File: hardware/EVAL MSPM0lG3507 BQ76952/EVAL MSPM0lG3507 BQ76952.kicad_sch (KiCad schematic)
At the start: 68 parts, among them J1 Conn_01x09_Socket, J10 Screw_Terminal_01x02, J11 Screw_Terminal_01x02, J12 Screw_Terminal_01x02, J13 Screw_Terminal_01x02, J14 Screw_Terminal_01x02, J17 Conn_02x02_Odd_Even, J2 Conn_02x05_Odd_Even, J3 Conn_01x04_Pin, J4 Screw_Terminal_01x02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

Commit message: partial correctinos to kicad
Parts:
- removed D6: LED, LED_SMD:LED_0805_2012Metric_Pad1.15x1.40mm_HandSolder, symbol Device:LED
- added D4: LED, LED_SMD:LED_0603_1608Metric, symbol Device:LED
- D1: footprint LED_SMD:LED_0201_0603Metric_Pad0.64x0.40mm_HandSolder -> LED_SMD:LED_0603_1608Metric; unit x10 0.12 -> 0.118
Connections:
- net -BATT: now also D4.1 (K)
- net at R3.2: now also D4.2 (A)
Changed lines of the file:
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@@
 			)
 		)
-		(property "Footprint" "LED_SMD:LED_0201_0603Metric_Pad0.64x0.40mm_HandSolder"
+		(property "Footprint" "LED_SMD:LED_0603_1608Metric"
 			(at 137.16 55.88 0)
 			(effects
@@
 			)
 		)
-		(property "unit x10" "0.12"
+		(property "unit x10" "0.118"
 			(at 137.16 55.88 90)
 			(effects
@@
 	)
 	(symbol
+		(lib_id "Device:LED")
+		(at 303.53 123.19 90)
+		(unit 1)
+		(exclude_from_sim no)
+		(in_bom yes)
+		(on_board yes)
+		(dnp no)
+		(property "Reference" "D4"
+			(at 307.34 122.174 90)
+			(effects
+				(font
+					(size 1.27 1.27)
+				)
+			)
+		)
+		(property "Value" "LED"
+			(at 307.34 124.714 90)
+			(effects
+				(font
+					(size 1.27 1.27)
+				)
+			)
+		)
+		(property "Footprint" "LED_SMD:LED_0603_1608Metric"
+			(at 303.53 123.19 0)
+			(effects
+				(font
+					(size 1.27 1.27)
+				)
+				(hide yes)
+			)
+		)
+		(property "Datasheet" ""
+			(at 303.53 123.19 0)
+			(effects
+				(font
+					(size 1.27 1.27)
+				)
+				(hide yes)
+			)
+		)
+		(property "Description" "Amber LED, 5mA, 1.9Vf, 5Vr, 75mW"
+			(at 303.53 123.19 0)
+			(effects
+				(font
+					(size 1.27 1.27)
+				)
+				(hide yes)
+			)
+		)
+		(property "Sim.Pins" "1=K 2=A"
+			(at 303.53 123.19 0)
+			(effects
+				(font
+					(size 1.27 1.27)
+				)
+				(hide yes)
+			)
+		)
+		(property "Sim.Device" ""
+			(at 303.53 123.19 90)
+			(effects
+				(font
+					(size 1.27 1.27)
+				)
+				(hide yes)
+			)
+		)
+		(property "Sim.Type" ""
+			(at 303.53 123.19 90)
+			(effects
+				(font
+					(size 1.27 1.27)
+				)
+				(hide yes)
+			)
+		)
+		(property "mouser" "https://www.mouser.com/ProductDetail/Inolux/IN-S63AT5A?qs=sGAEpiMZZMusoohG2hS%252B168PbK3Wnfgfrs6xlVjjR%2FyR990S%252B53E4A%3D%3D"
+			(at 303.53 123.19 90)
+			(effects
+				(font
+					(size 1.27 1.27)
+				)
+				(hide yes)
+			)
+		)
+		(property "specs" "amber, 5mA, 1.9V, 75mW, -40C, +85C"
+			(at 303.53 123.19 90)
+			(effects
+				(font
+					(size 1.27 1.27)
+				)
+				(hide yes)
+			)
+		)
+		(property "unit x10" "0.118"
+			(at 303.53 123.19 90)
+			(effects
+				(font
+					(size 1.27 1.27)
+				)
+				(hide yes)
+			)
+		)
+		(pin "2"
+		)
+		(pin "1"
+		)
+		(instances
+			(project "EVAL MSPM0lG3507 BQ76952"
+				(path "/20ac6af0-79b5-4ba6-aad3-75081d02c913"
+					(reference "D4")
+					(unit 1)
+				)
+			)
+		)
+	)
+	(symbol
 		(lib_id "power:+3.3V")
 		(at 133.35 44.45 90)
@@
 					(unit 1)
 				)
-			)
-		)
-	)
-	(symbol
-		(lib_id "Device:LED")
-		(at 303.53 123.19 90)
-		(unit 1)
-		(exclude_from_sim no)
-		(in_bom yes)
-		(on_board yes)
-		(dnp no)
-		(property "Reference" "D6"
-			(at 307.086 121.92 90)
-			(effects
-				(font
-					(size 1.27 1.27)
-				)
-			)
-		)
-		(property "Value" "LED"
-			(at 307.086 124.46 90)
-			(effects
-				(font
-					(size 1.27 1.27)
-				)
-			)
-		)
-		(property "Footprint" "LED_SMD:LED_0805_2012Metric_Pad1.15x1.40mm_HandSolder"
-			(at 303.53 123.19 0)
-			(effects
-				(font
-					(size 1.27 1.27)
-				)
-				(hide yes)
-			)
-		)
-		(property "Datasheet" "https://www.mouser.com/ProductDetail/Bivar/SM0603GCL?qs=sGAEpiMZZMv0DJfhVcWlK3SnxywvxwccsLOn6MrrOhpuNHkjdeX7ag%3D%3D"
-			(at 303.53 123.19 0)
-			(effects
-				(font
-					(size 1.27 1.27)
-				)
-				(hide yes)
-			)
-		)
-		(property "Description" "Green LED, 2mA, 1.9Vf, 5Vr, 75mW"
-			(at 303.53 123.19 0)
-			(effects
-				(font
-					(size 1.27 1.27)
-				)
-				(hide yes)
-			)
-		)
-		(property "Sim.Pins" "1=K 2=A"
-			(at 303.53 123.19 0)
-			(effects
-				(font
-					(size 1.27 1.27)
-				)
-				(hide yes)
-			)
-		)
-		(property "Sim.Device" ""
-			(at 303.53 123.19 90)
-			(effects
-				(font
-					(size 1.27 1.27)
-				)
-				(hide yes)
-			)
-		)
-		(property "Sim.Type" ""
-			(at 303.53 123.19 90)
-			(effects
-				(font
-					(size 1.27 1.27)
-				)
-				(hide yes)
-			)
-		)
-		(property "mouser" "https://www.mouser.com/ProductDetail/Bivar/SM0603GCL?qs=sGAEpiMZZMv0DJfhVcWlK3SnxywvxwccsLOn6MrrOhpuNHkjdeX7ag%3D%3D"
-			(at 303.53 123.19 90)
-			(effects
-				(font
-					(size 1.27 1.27)
-				)
-				(hide yes)
-			)
-		)
-		(property "specs" "green, 2mA, 1.9V, 78mW, -30C, +80C"
-			(at 303.53 123.19 90)
-			(effects
-				(font
-					(size 1.27 1.27)
-				)
-				(hide yes)
-			)
-		)
-		(property "unit x10" "0.42"
-			(at 303.53 123.19 90)
-			(effects
-				(font
-					(size 1.27 1.27)
-				)
-				(hide yes)
-			)
-		)
-		(pin "2"
-		)
-		(pin "1"
-		)
-		(instances
-			(project "VT MSPM0lG3507 BQ7962 layout test"
-				(path "/20ac6af0-79b5-4ba6-aad3-75081d02c913"
-					(reference "D6")
-					(unit 1)
-				)

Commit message: asdd
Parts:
- removed TP24, TP26: TestPoint, TestPoint:TestPoint_Loop_D2.50mm_Drill1.0mm_LowProfile, symbol Connector:TestPoint
- added C7: 220n, Capacitor_SMD:C_1206_3216Metric_Pad1.33x1.80mm_HandSolder, symbol Device:C_Small
- added TP2: TestPoint, TestPoint:TestPoint_Loop_D2.50mm_Drill1.0mm_LowProfile, symbol Connector:TestPoint
- R3, R6: value 700 -> 750; mouser (none) -> https://www.mouser.com/ProductDetail/YAGEO/RC1206JR-13750RL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; specs (none) -> 750mOhm, 250mW, 5%, 100PPM, 200C, -55C, +155C; unit x10 (none) -> 0.022
- SW1, SW2: mouser (none) -> https://www.mouser.com/ProductDetail/CK/KSC251J-SP-DELTA-LF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; unit x10 (none) -> 0.532
- TH1, TH2, TH3, TH4, TH5, TH6, TH7, TH8, TH9: now not fitted
- U2: mouser (none) -> https://www.mouser.com/ProductDetail/595-MSPM0G3507SPMR; unit x10 (none) -> 1.81
- U6, U7: now not fitted; now left out of the parts list
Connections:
- net +3.3V: now also C7.1
- net -BATT: now also C7.2
- net at U2.64 (PB12): now also TP2.1
- net PA0: no longer names the net of U2.33 (PA0)
- net PA1: no longer names the net of U2.34 (PA1)
- net PB26: no longer names the net of U2.28 (PB26)
- no-connect marks 57 -> 60
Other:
- note added: "2.1"
- note added: "limited active balancing. big cap on COM, one hot encoding. ic is $30 though, make alternative"
- note removed: "2"

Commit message: sGDdfsddsf
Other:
- note added: "10k required"
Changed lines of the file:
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@@
+		)
+	)
+	(text "10k required"
+		(exclude_from_sim no)
+		(at 87.63 123.444 90)
+		(effects
+			(font
+				(size 1.27 1.27)
+			)
 		)
 	)

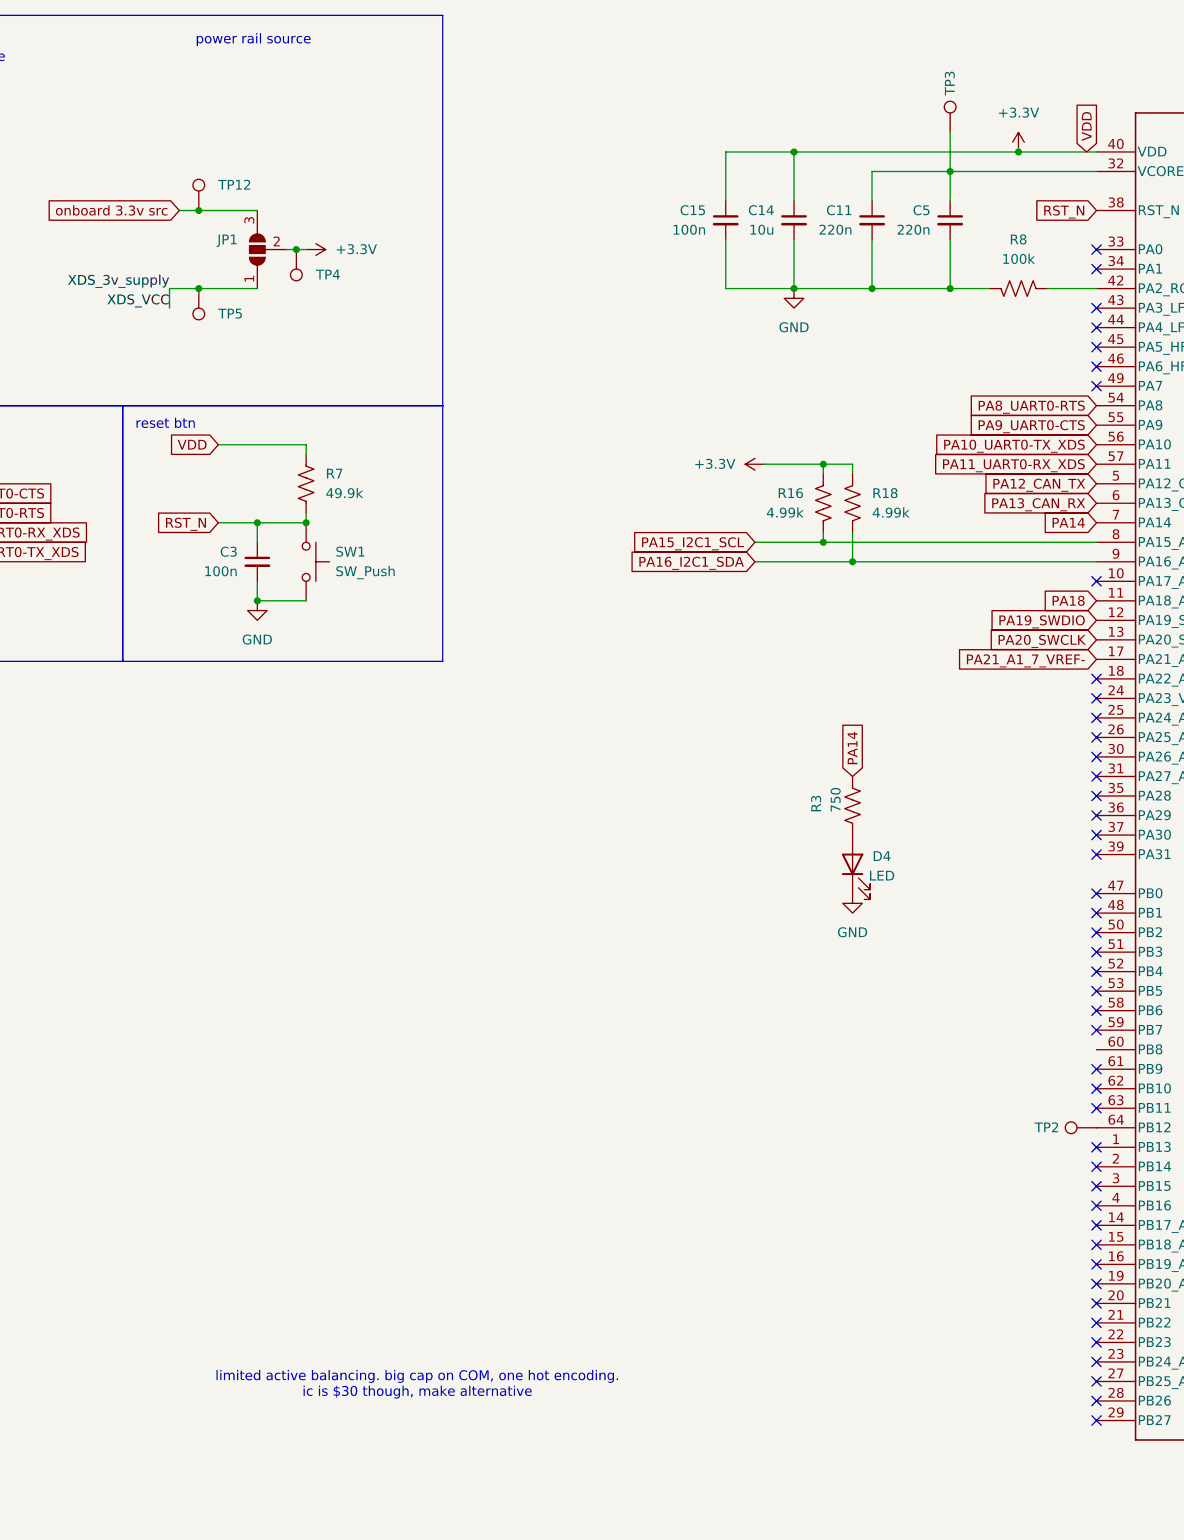
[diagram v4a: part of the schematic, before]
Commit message: corrected CAN transceiver parts
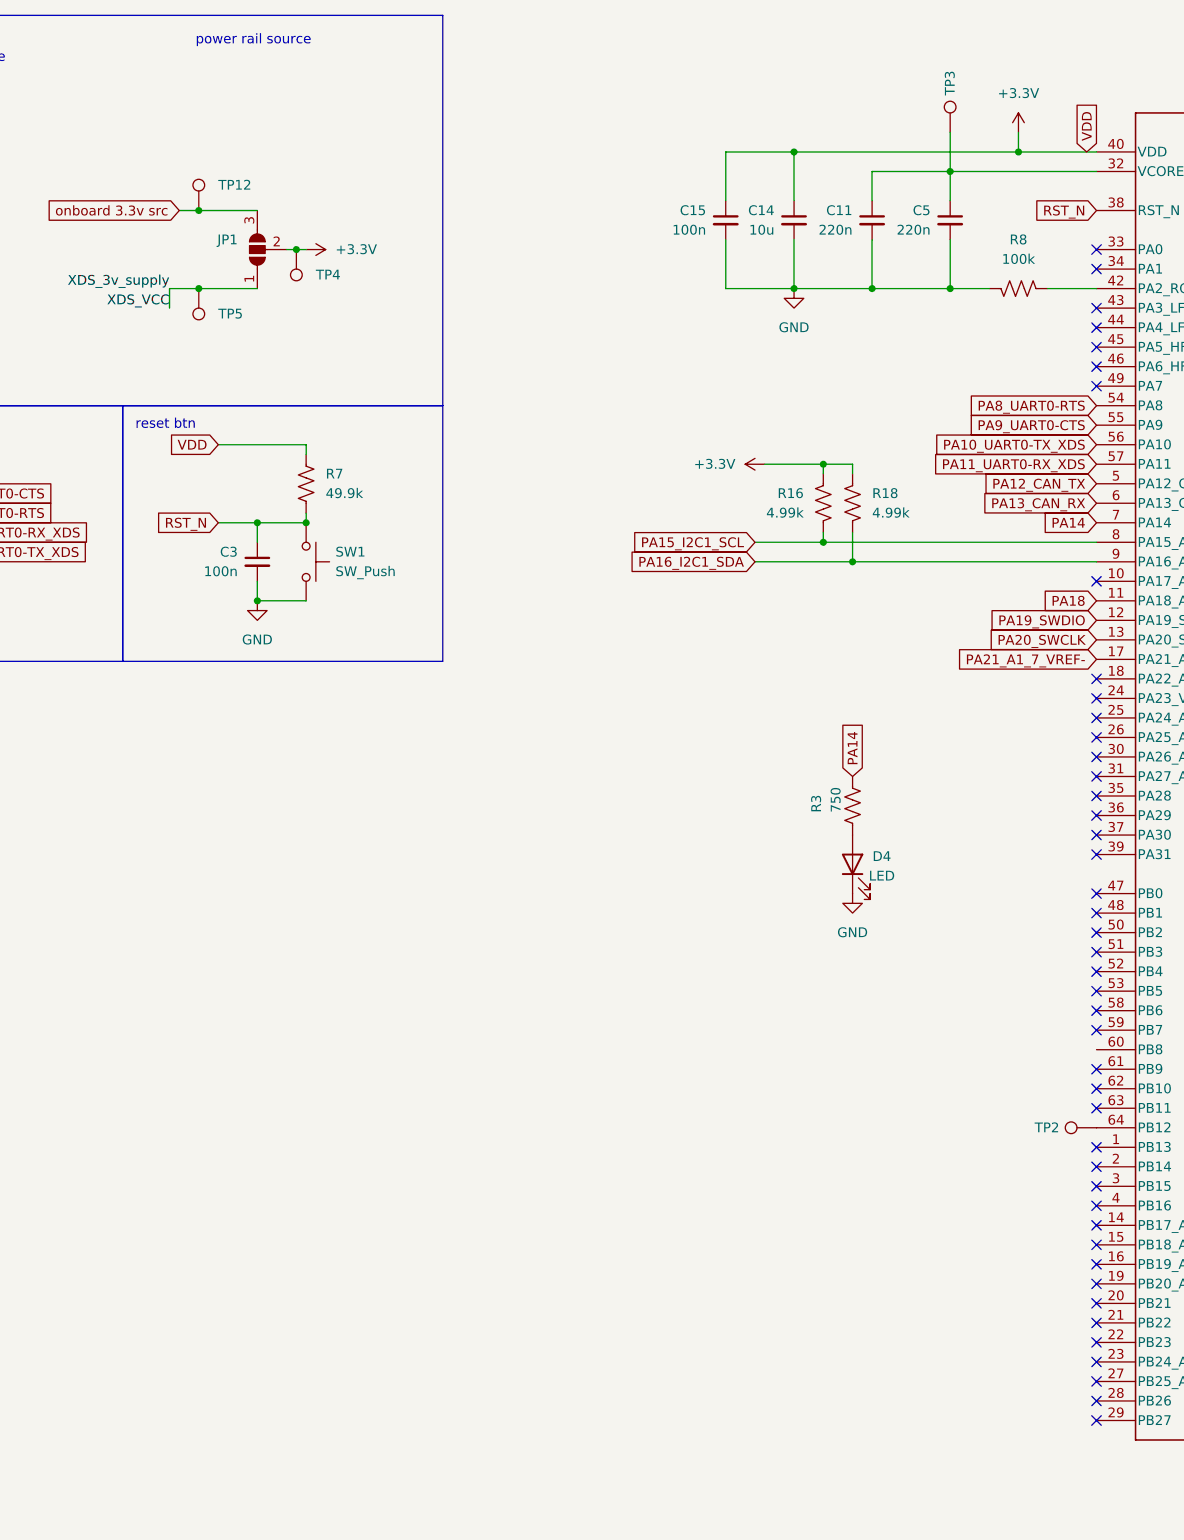
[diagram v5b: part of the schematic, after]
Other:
- note removed: "limited active balancing. big cap on COM, one hot encoding. ic is $30 though, make alternative"

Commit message: bluhhh
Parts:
- removed R10, R13, R14: 4.99k, Resistor_SMD:R_1206_3216Metric_Pad1.30x1.75mm_HandSolder, symbol Device:R_US
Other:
- sheet BQ76952 16C ports: added none; removed LD, PACK
- note added: "high=shutdown"
- note removed: "10k required"

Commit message: d
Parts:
- J1, J17, J3, J5, J6: mouser (none) -> https://www.mouser.com/ProductDetail/3M-Electronic-Solution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
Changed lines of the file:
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@@
 			)
 		)
+		(property "mouser" "https://www.mouser.com/ProductDetail/3M-Electronic-Solutions-Division/929400-01-07-RK?qs=8Li5tweT5mxAnRwvBSG7wg%3D%3D&mgh=1&utm_id=22693461723&utm_source=google&utm_medium=cpc&utm_marketing_tactic=amercorp&gad_source=1&gad_campaignid=22699465430&gclid=Cj0KCQjw0Y3HBhCxARIsAN7931V3Q9lNZD5h4uJjA3G07-TRSv1KPKk1_9nCCKxyCRbpuWAP8GWV0v4aAg3GEALw_wcB"
+			(at 123.19 127 90)
+			(effects
+				(font
+					(size 1.27 1.27)
+				)
+				(hide yes)
+			)
+		)
 		(pin "1"
 		)
@@
 			)
 		)
+		(property "mouser" "https://www.mouser.com/ProductDetail/3M-Electronic-Solutions-Division/929400-01-07-RK?qs=8Li5tweT5mxAnRwvBSG7wg%3D%3D&mgh=1&utm_id=22693461723&utm_source=google&utm_medium=cpc&utm_marketing_tactic=amercorp&gad_source=1&gad_campaignid=22699465430&gclid=Cj0KCQjw0Y3HBhCxARIsAN7931V3Q9lNZD5h4uJjA3G07-TRSv1KPKk1_9nCCKxyCRbpuWAP8GWV0v4aAg3GEALw_wcB"
+			(at 163.83 83.82 0)
+			(effects
+				(font
+					(size 1.27 1.27)
+				)
+				(hide yes)
+			)
+		)
 		(pin "4"
 		)
@@
 			)
 		)
+		(property "mouser" "https://www.mouser.com/ProductDetail/3M-Electronic-Solutions-Division/929400-01-07-RK?qs=8Li5tweT5mxAnRwvBSG7wg%3D%3D&mgh=1&utm_id=22693461723&utm_source=google&utm_medium=cpc&utm_marketing_tactic=amercorp&gad_source=1&gad_campaignid=22699465430&gclid=Cj0KCQjw0Y3HBhCxARIsAN7931V3Q9lNZD5h4uJjA3G07-TRSv1KPKk1_9nCCKxyCRbpuWAP8GWV0v4aAg3GEALw_wcB"
+			(at 24.13 59.69 0)
+			(effects
+				(font
+					(size 1.27 1.27)
+				)
+				(hide yes)
+			)
+		)
 		(pin "4"
 		)
@@
 			)
 		)
+		(property "mouser" "https://www.mouser.com/ProductDetail/3M-Electronic-Solutions-Division/929400-01-07-RK?qs=8Li5tweT5mxAnRwvBSG7wg%3D%3D&mgh=1&utm_id=22693461723&utm_source=google&utm_medium=cpc&utm_marketing_tactic=amercorp&gad_source=1&gad_campaignid=22699465430&gclid=Cj0KCQjw0Y3HBhCxARIsAN7931V3Q9lNZD5h4uJjA3G07-TRSv1KPKk1_9nCCKxyCRbpuWAP8GWV0v4aAg3GEALw_wcB"
+			(at 91.44 171.45 0)
+			(effects
+				(font
+					(size 1.27 1.27)
+				)
+				(hide yes)
+			)
+		)
 		(pin "4"
 		)
@@
 			(at 113.03 135.89 0)
 			(effects
+				(font
+					(size 1.27 1.27)
+				)
+				(hide yes)
+			)
+		)
+		(property "mouser" "https://www.mouser.com/ProductDetail/3M-Electronic-Solutions-Division/929400-01-07-RK?qs=8Li5tweT5mxAnRwvBSG7wg%3D%3D&mgh=1&utm_id=22693461723&utm_source=google&utm_medium=cpc&utm_marketing_tactic=amercorp&gad_source=1&gad_campaignid=22699465430&gclid=Cj0KCQjw0Y3HBhCxARIsAN7931V3Q9lNZD5h4uJjA3G07-TRSv1KPKk1_9nCCKxyCRbpuWAP8GWV0v4aAg3GEALw_wcB"
+			(at 113.03 135.89 0)
+			(effects

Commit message: ac;lkacnl;
acea;kca
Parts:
- removed U6, U7: TPD4E05U06DQA, Package_SON:USON-10_2.5x1.0mm_P0.5mm, symbol Power_Protection:TPD4E05U06DQA
- J2: now fitted; now in the parts list
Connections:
- no-connect marks 60 -> 51
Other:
- note removed: "BLS invoke (will use later on)"
- note removed: "JTAG"
- note removed: "TVS"
- note removed: "XDS"
- note removed: "not really a 3v3 solution but this'll catch most other things TODO: get one thats for 3v3 signals"
- moved on the sheet: J1
